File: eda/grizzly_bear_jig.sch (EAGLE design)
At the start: 28 parts, among them Q2 IRFML8244, U1 ISL83491SOIC, U2 ATTINY1634

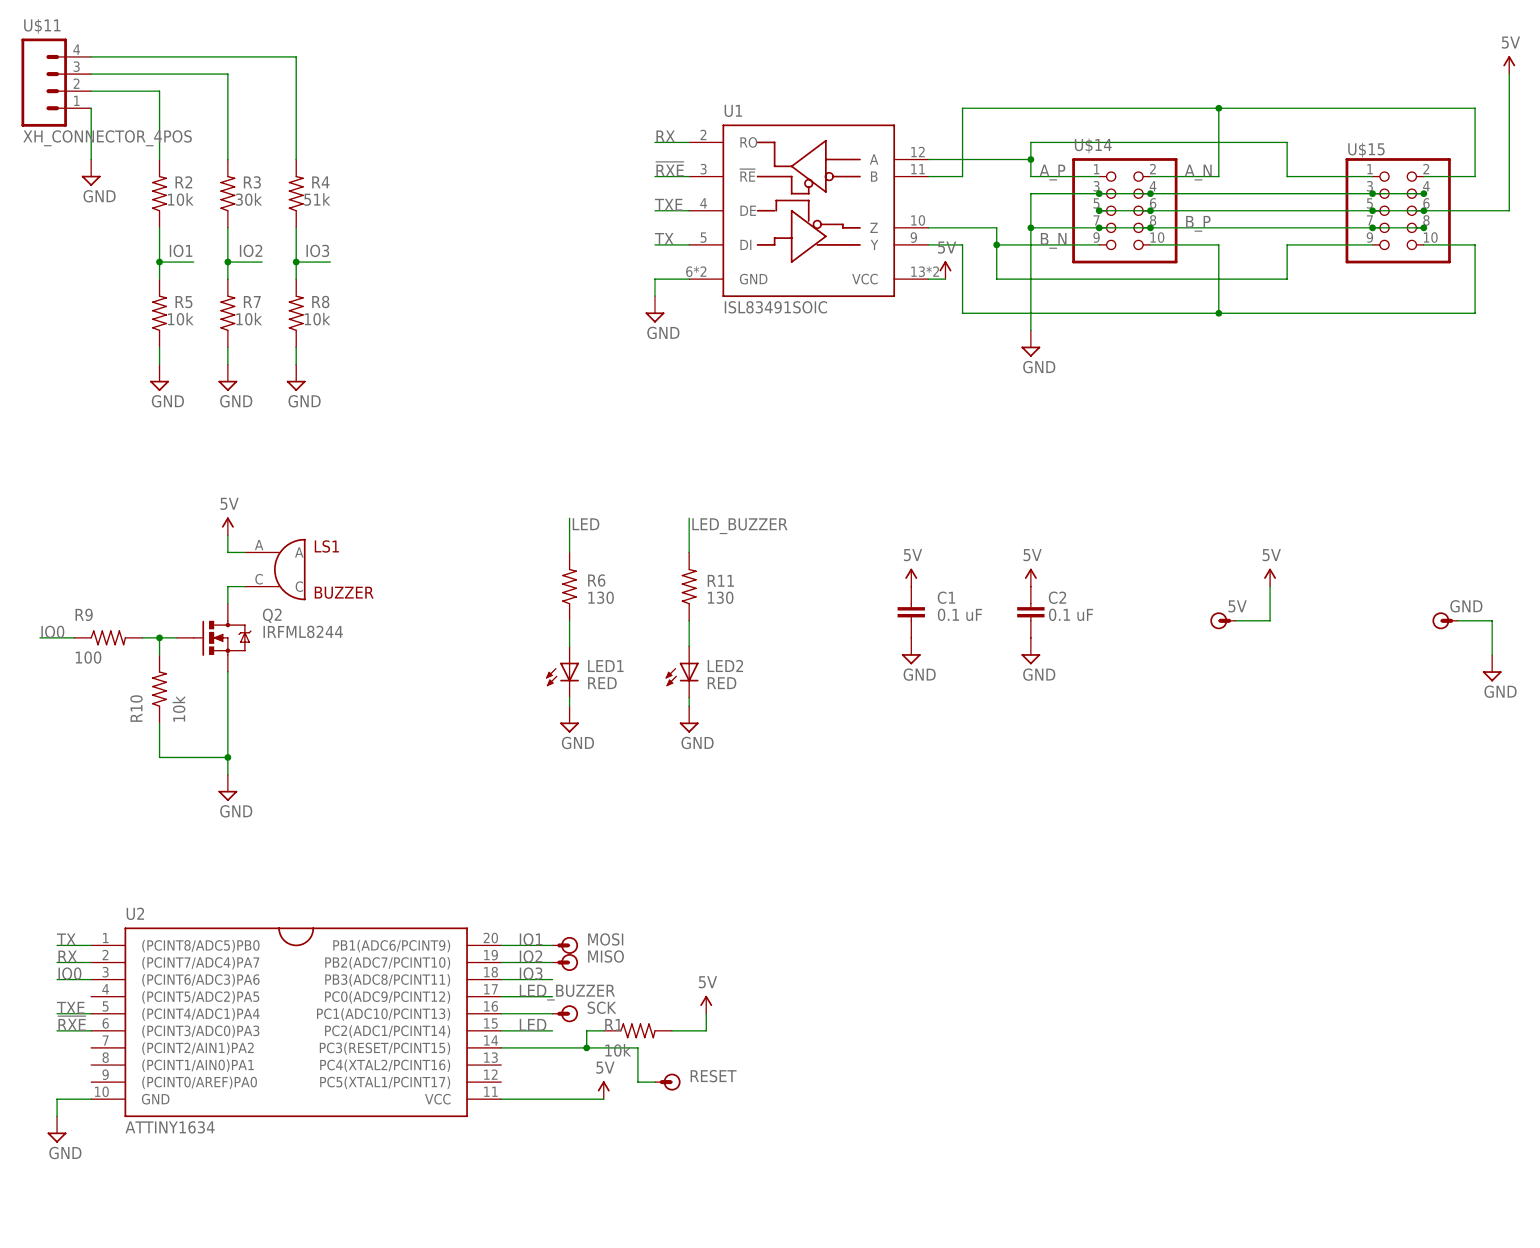
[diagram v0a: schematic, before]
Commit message: Rerouted to accomodate 2x5 shrouded connector. On battery_buzzer, grizzly_bear, smartsensor, smartsensor_powered, and team_flag. Thanks Doug and Yizhe for helping!
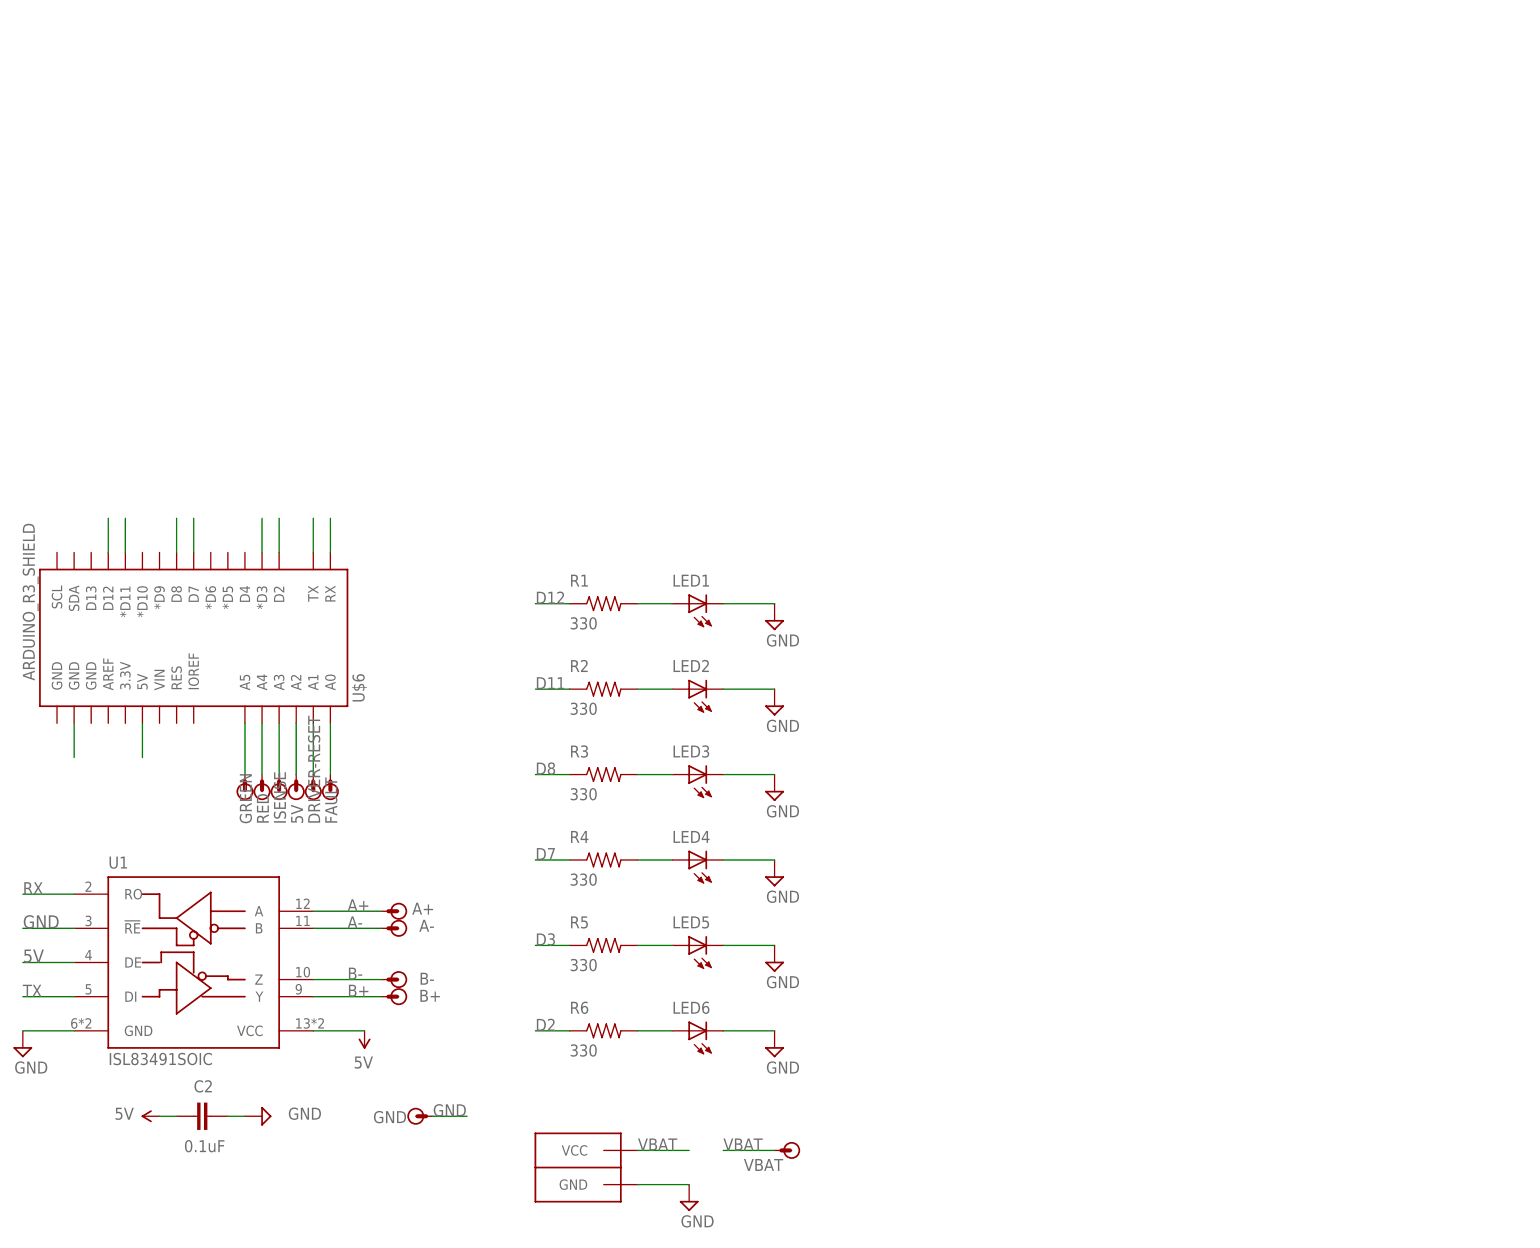
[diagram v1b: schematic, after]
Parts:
- removed C1: 0.1 uF, pie:CAP0603-CAP
- removed LS1: BUZZER, pie:BUZZER
- removed MISO, MOSI, RESET, SCK: (no value), pie:POGO_PIN
- removed Q2: IRFML8244, pie:MOSFET-NCHANNELSMD
- removed R10, R7, R8: 10k, pie:R-US_R0603
- removed R11: 130, pie:R-US_R0603
- removed R9: 100, pie:R-US_R0603
- removed U$11: XH_CONNECTOR_4POS, pie:XH_CONNECTOR_4POS
- removed U$14: (no value), pie:SENSOR_CON_5PINPTH-SHROUDED
- removed U$15: (no value), pie:SENSOR_CON_5PINSMD-EDGE
- removed U2: ATTINY1634, pie:ATTINY1634
- added A+, A-, B+, B-, DRIVER-RESET, FAULT, GREEN, ISENSE, RED, VBAT: (no value), pie:POGO_PIN
- added CONN1: ANDERSONHORIZONTAL, pie:ANDERSONHORIZONTAL
- added LED3, LED4, LED5, LED6: (no value), pie:LED0805
- added U$6: ARDUINO_R3_SHIELD, SparkFun-Boards:ARDUINO_R3_SHIELD
- C2: value 0.1 uF -> 0.1uF; device pie:CAP0603-CAP -> SparkFun-Capacitors:0.1UF-25V(+80/-20%)(0603)
- LED1, LED2: value RED -> (none)
- R1, R2, R5: value 10k -> 330
- R3: value 30k -> 330
- R4: value 51k -> 330
- R6: value 130 -> 330
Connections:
- removed net !RXE: U1.!RE, U2.(PCINT3/ADC0)PA3
- removed net A_N: U$14.2, U$15.2, U1.B
- removed net A_P: U$14.1, U$15.1, U1.A
- removed net B_N: U$14.9, U$15.9, U1.Z
- removed net B_P: U$14.10, U$15.10, U1.Y
- removed net IO0: R9.1, U2.(PCINT6/ADC3)PA6
- removed net IO1: MOSI.P$1, R2.1, R5.2, U2.PB1(ADC6/PCINT9)
- removed net IO2: MISO.P$1, R3.1, R7.2, U2.PB2(ADC7/PCINT10)
- removed net IO3: R4.1, R8.2, U2.PB3(ADC8/PCINT11)
- removed net LED: R6.2, U2.PC2(ADC1/PCINT14)
- removed net LED_BUZZER: R11.2, U2.PC0(ADC9/PCINT12)
- removed net RESET: R1.1, RESET.P$1, U2.PC3(RESET/PCINT15)
- removed net TXE: U1.DE, U2.(PCINT4/ADC1)PA4
- new net A+: A+.P$1, U1.A
- new net A-: A-.P$1, U1.B
- new net B+: B+.P$1, U1.Y
- new net B-: B-.P$1, U1.Z
- new net D11: R2.1, U$6.*D11
- new net D12: R1.1, U$6.D12
- new net D2: R6.1, U$6.D2
- new net D3: R5.1, U$6.*D3
- new net D7: R4.1, U$6.D7
- new net D8: R3.1, U$6.D8
- new net N$10: LED3.A, R3.2
- new net N$11: LED4.A, R4.2
- new net N$13: FAULT.P$1, U$6.A0
- new net N$9: LED2.A, R2.2
- new net VBAT: CONN1.VCC, VBAT.P$1
- net 5V: now also U$6.5V, U1.DE; no longer 5V.P$1, C1.1, LS1.A, R1.2, U$14.5, U$14.6, U$15.5, U$15.6, U2.VCC
- net GND: now also CONN1.GND, LED3.C, LED4.C, LED5.C, LED6.C, U$6.GND@1, U1.!RE; no longer C1.2, Q2.S, R10.1, R5.1, R7.1, R8.1, U$11.1, U$14.3, U$14.4, U$14.7, U$14.8, U$15.3, U$15.4, U$15.7, U$15.8, U2.GND
- net N$1: now also LED5.A, R5.2; no longer R2.2, U$11.2
- net N$2: now also LED6.A, R6.2; no longer R3.2, U$11.3
- net N$3: now also GREEN.P$1, U$6.A5; no longer LED1.A, R6.1
- net N$4: now also RED.P$1, U$6.A4; no longer R4.2, U$11.4
- net N$5: now also ISENSE.P$1, U$6.A3; no longer LS1.C, Q2.D
- net N$6: now also 5V.P$1, U$6.A2; no longer Q2.G, R10.2, R9.2
- net N$7: now also DRIVER-RESET.P$1, U$6.A1; no longer LED2.A, R11.1
- net N$8: now also LED1.A, R1.2; no longer SCK.P$1, U2.PC1(ADC10/PCINT13)
- net RX: now also U$6.RX; no longer U2.(PCINT7/ADC4)PA7
- net TX: now also U$6.TX; no longer U2.(PCINT8/ADC5)PB0
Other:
- moved on the sheet: 5V, C2, GND, LED1, LED2, R1, R2, R3, R4, R5, R6, U1
